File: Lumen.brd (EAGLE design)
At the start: 59.6 x 24 mm, 25 parts, among them J1 AVR_SPI_PRG_6PTH, U1 Tiny45-20-SMT, Y1 8MHZ

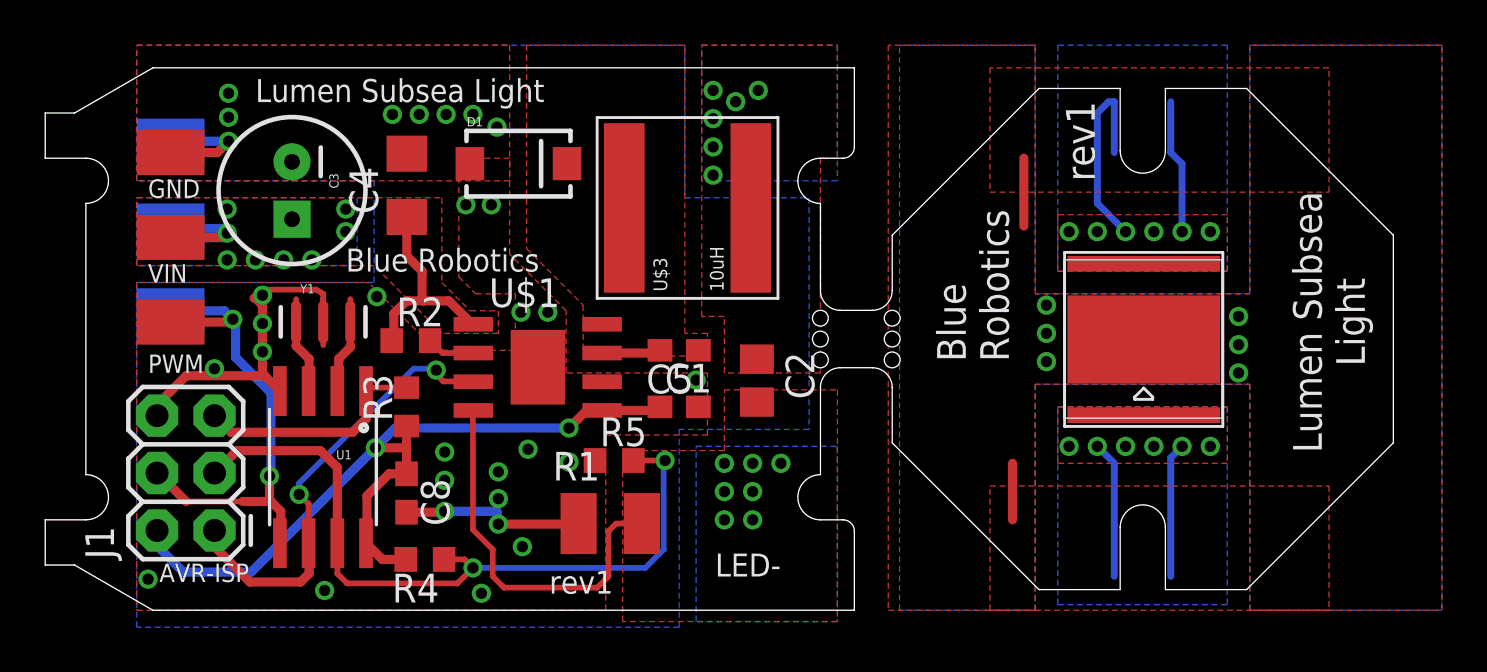
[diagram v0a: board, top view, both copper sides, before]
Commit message: Fixed a lot of little things. Added regulator back into the design. Upgrade capacitor voltage ratings.
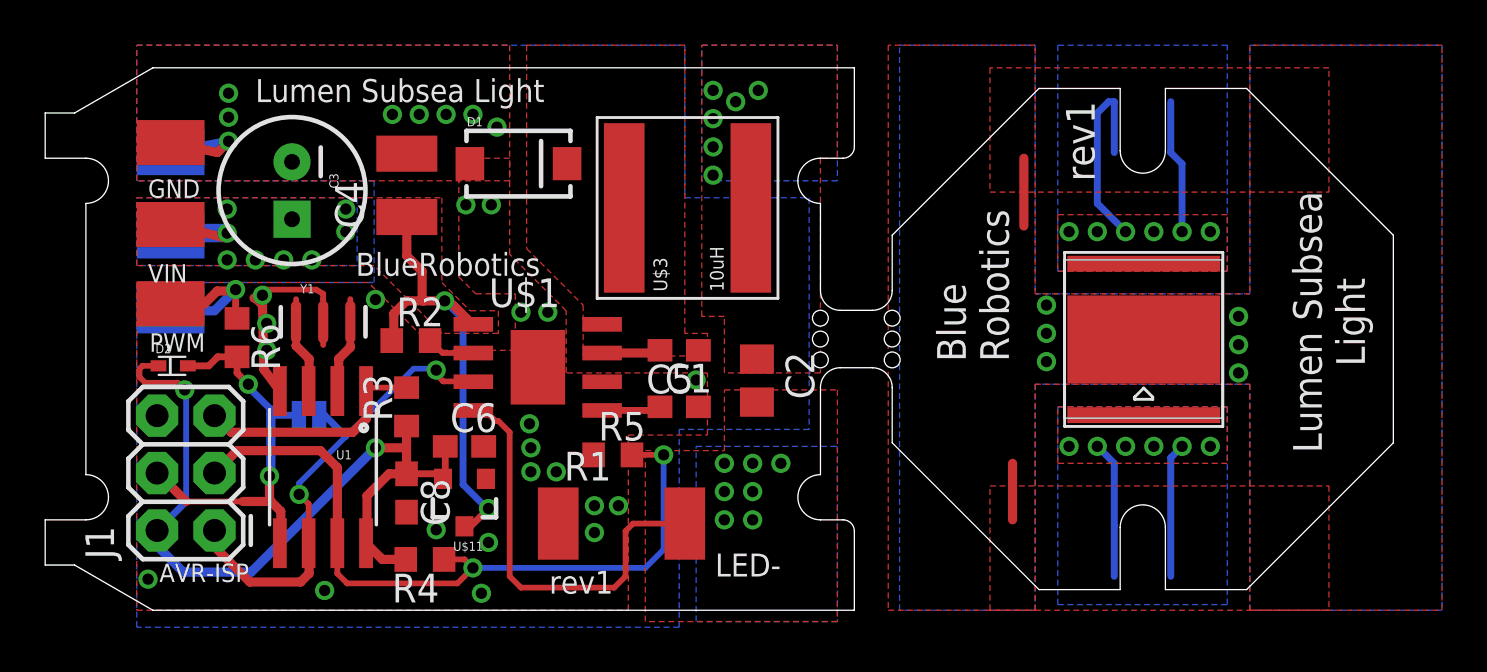
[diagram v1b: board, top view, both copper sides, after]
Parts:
- added C6: 10uF, resistor:C0603
- added D2: (no value), SparkFun-DiscreteSemi:SOD523
- added R6: 27K, resistor:R0603
- added SJ1: JUMPER-PAD-2-NO, SparkFun-Passives:PAD-JUMPER-2-NO_NO_SILK
- added U$11: VREG-ZXTR2105, BlueRobotics-Main:SOT23-3
- C2: value 0.68uF 50V -> 0.68uF 100V
- C4: value 4.7uF 50V -> 4.7uF 80V; device resistor:C1206 -> resistor:C1210
- D1: value 50V 3A -> 60V 3A
- R1: value 0.068 1W -> 0.082 1W; device resistor:R1210 -> resistor:R2512
- moved U$7 0.81 mm to (3.75, 13.6)
- moved U$8 0.56 mm to (3.75, 17.1)
- moved R1 0.50 mm to (23.7, 3.83)
- moved U$6 0.50 mm to (3.75, 20.2)
- moved U$5 0.44 mm to (3.75, 16.6)
- moved U$9 0.44 mm to (3.75, 20.7)
- moved R5 0.26 mm to (23.3, 6.88)
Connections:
- new net SIGNAL_HV: R6.1, U$4.P$1, U$7.P$1
- new net VCC6211: C1.1, U$1.5
- net GND: now also C6.2, U$11.1
- net LED-PWM: now also SJ1.2
- net SIGNAL: now also D2.A, R6.2, SJ1.1; no longer U$4.P$1, U$7.P$1
- net VCC: now also C6.1, D2.C, U$11.2; no longer C1.1, U$1.5
- net VIN: now also U$11.3
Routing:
- net GND: track 27.3 -> 13.9 mm, vias 30 -> 29
- net VIN: track 14.6 -> 27.7 mm, vias 8 -> 10
- net SIGNAL_HV: track 0.00 -> 7.70 mm, vias 0 -> 1
- net SIGNAL: track 22.1 -> 18.3 mm
- net VCC6211: track 0.00 -> 2.63 mm
- net LED-: track 16.9 -> 18.9 mm
- net LED-PWM: track 20.0 -> 21.6 mm
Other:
- board text added: "BlueRobotics"
- board text added: "Direct Signal to A6211"

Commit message: Fixed some layout issues per John's suggestion. Added pads for a snubber that will probably not be populated.
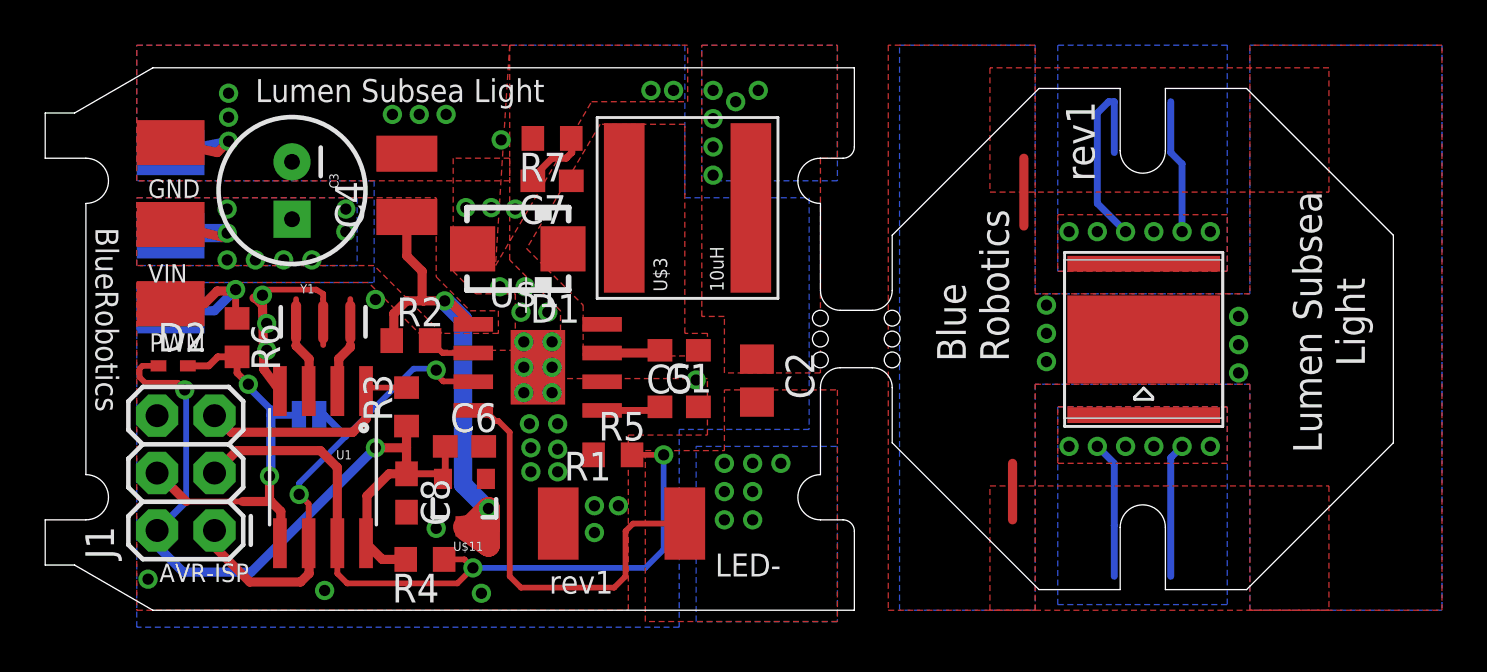
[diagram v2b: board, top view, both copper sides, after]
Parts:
- added C7: NP, resistor:C0603
- added R7: NP, resistor:R0603
- D1: device SparkFun-DiscreteSemi:SMA-DIODE -> BlueRobotics-Main:SMA
- D2: value (none) -> BAT54; device SparkFun-DiscreteSemi:SOD523 -> BlueRobotics-Main:SOD523
- moved D1 3.77 mm to (19.1, 16.0), turned to 180 degrees
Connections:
- new net N$2: C7.2, R7.1
- net GND: now also R7.2
- net N$5: now also C7.1
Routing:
- net VIN: track 27.7 -> 31.6 mm
- net N$2: track 0.00 -> 2.97 mm
- net GND: vias 29 -> 40
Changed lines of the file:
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@@
 <setting verticaltext="up"/>
 </settings>
-<grid distance="5" unitdist="mm" unit="mm" style="lines" multiple="1" display="yes" altdistance="0.0625" altunitdist="mm" altunit="mm"/>
+<grid distance="5" unitdist="mm" unit="mm" style="lines" multiple="1" display="yes" altdistance="0.125" altunitdist="mm" altunit="mm"/>
 <layers>
 <layer number="1" name="Top" color="4" fill="1" visible="yes" active="yes"/>
@@
 <text x="7.5" y="23.5" size="1.016" layer="21" align="top-left">Lumen Subsea Light</text>
 <text x="20.5" y="1.75" size="1.016" layer="21" align="top-left">rev1</text>
-<text x="11.9375" y="15.8125" size="1.016" layer="21" align="top-left">BlueRobotics</text>
+<text x="1.4375" y="16.9375" size="1.016" layer="21" rot="SR270" align="top-left">BlueRobotics</text>
 <text x="48" y="6.25" size="1.016" layer="22" rot="MR0" align="top-left">LED-</text>
 <text x="45.5" y="17.75" size="1.016" layer="22" rot="SMR180" align="top-left">LED+</text>
@@
 <element name="C4" library="resistor" package="C1210" value="4.7uF 80V" x="14.2" y="18.8" rot="R90"/>
 <element name="C5" library="resistor" package="C0603" value="0.1uF" x="26.25" y="11.5" rot="R180"/>
-<element name="D1" library="SparkFun-DiscreteSemi" package="SMA-DIODE" value="60V 3A" x="19.14" y="19.76">
-<attribute name="PROD_ID" value="DIO-09886" x="19.14" y="19.76" size="1.778" layer="27" display="off"/>
-</element>
+<element name="D1" library="BlueRobotics-Main" package="SMA" value="60V 3A" x="19.11" y="15.99" rot="R180"/>
 <element name="J1" library="SparkFun-Connectors" package="2X3" value="AVR_SPI_PRG_6PTH" x="5.69" y="3.53" smashed="yes" rot="R90">
 <attribute name="NAME" x="1.245" y="2.26" size="1.27" layer="25" ratio="10" rot="R90"/>
@@
 <element name="C6" library="resistor" package="C0603" value="10uF" x="16.75" y="7.25"/>
 <element name="SJ1" library="SparkFun-Passives" package="PAD-JUMPER-2-NO_NO_SILK" value="JUMPER-PAD-2-NO" x="9.875" y="8.625" rot="MR180"/>
-<element name="D2" library="SparkFun-DiscreteSemi" package="SOD523" value="" x="3.8125" y="10.8125"/>
+<element name="D2" library="BlueRobotics-Main" package="SOD523" value="BAT54" x="3.8125" y="10.8125"/>
 <element name="R6" library="resistor" package="R0603" value="27K" x="6.6875" y="12.0625" rot="R270"/>
+<element name="C7" library="resistor" package="C0603" value="NP" x="20.625" y="19" rot="R180"/>
+<element name="R7" library="resistor" package="R0603" value="NP" x="20.625" y="20.875" rot="R180"/>
 </elements>
 <signals>
@@
 <wire x1="6.3125" y1="20.75" x2="3.75" y2="20.25" width="0.4064" layer="16"/>
 <via x="13.5625" y="21.9375" extent="1-16" drill="0.5"/>
-<via x="17.125" y="21.9375" extent="1-16" drill="0.5"/>
+<via x="18.375" y="20.8125" extent="1-16" drill="0.5"/>
 <via x="14.75" y="21.9375" extent="1-16" drill="0.5"/>
 <via x="15.9375" y="21.9375" extent="1-16" drill="0.5"/>
-<via x="18.1875" y="21.375" extent="1-16" drill="0.5"/>
-<via x="16.8125" y="17.9375" extent="1-16" drill="0.5"/>
-<via x="17.9375" y="17.9375" extent="1-16" drill="0.5"/>
+<via x="16.8125" y="17.8125" extent="1-16" drill="0.5"/>
+<via x="17.9375" y="17.8125" extent="1-16" drill="0.5"/>
 <via x="6.3125" y="21.8125" extent="1-16" drill="0.5"/>
 <via x="6.3125" y="22.875" extent="1-16" drill="0.5"/>
 <via x="12.8125" y="13.75" extent="1-16" drill="0.5"/>
 <via x="8" y="11.5" extent="1-16" drill="0.5"/>
-<via x="15.5" y="3.5625" extent="1-16" drill="0.5"/>
+<via x="15.5" y="3.625" extent="1-16" drill="0.5"/>
 <via x="22.5" y="3.4375" extent="1-16" drill="0.5"/>
 <via x="19.6875" y="7.1875" extent="1-16" drill="0.5"/>
@@
 <via x="17.5" y="0.75" extent="1-16" drill="0.5"/>
 <polygon width="0.4064" layer="1" isolate="0.254" thermals="no">
-<vertex x="16.5" y="20"/>
-<vertex x="16.5" y="14.75"/>
+<vertex x="16.25" y="20"/>
+<vertex x="16.25" y="15"/>
 <vertex x="17.25" y="14"/>
 <vertex x="19" y="14"/>
@@
 <vertex x="24" y="7.75"/>
 <vertex x="27.5" y="7.75"/>
-<vertex x="27.5" y="10.5"/>
-<vertex x="21.25" y="10.5"/>
-<vertex x="21.25" y="13.25"/>
-<vertex x="18.75" y="15.75"/>
+<vertex x="27.5" y="10.25"/>
+<vertex x="21" y="10.25"/>
+<vertex x="21" y="13.25"/>
+<vertex x="18.75" y="15.5"/>
 <vertex x="18.75" y="20"/>
 </polygon>
@@
 <via x="23.5625" y="4.625" extent="1-16" drill="0.5"/>
 <via x="19.625" y="8.25" extent="1-16" drill="0.5"/>
-<via x="17.8125" y="3" extent="1-16" drill="0.5"/>
 <contactref element="C6" pad="2"/>
-<via x="20.8125" y="6.125" extent="1-16" drill="0.5"/>
+<via x="20.875" y="6.125" extent="1-16" drill="0.5"/>
+<polygon width="0.3048" layer="1" isolate="0.254">
+<vertex x="18.125" y="15.25"/>
+<vertex x="22.375" y="22.5"/>
+<vertex x="26.625" y="22.5"/>
+<vertex x="26.625" y="25"/>
+<vertex x="18.75" y="25"/>
+</polygon>
+<via x="19" y="17.75" extent="1-16" drill="0.5"/>
+<via x="25" y="23" extent="1-16" drill="0.5"/>
+<via x="26" y="23" extent="1-16" drill="0.5"/>
+<via x="19.375" y="9.625" extent="1-16" drill="0.5"/>
+<via x="19.375" y="10.75" extent="1-16" drill="0.5"/>
+<via x="19.375" y="11.875" extent="1-16" drill="0.5"/>
+<via x="20.625" y="11.875" extent="1-16" drill="0.5"/>
+<via x="20.625" y="10.75" extent="1-16" drill="0.5"/>
+<via x="20.625" y="9.625" extent="1-16" drill="0.5"/>
+<via x="20.875" y="8.25" extent="1-16" drill="0.5"/>
+<via x="20.875" y="7.125" extent="1-16" drill="0.5"/>
+<via x="19.4375" y="14.3125" extent="1-16" drill="0.5"/>
+<via x="18.3125" y="14.3125" extent="1-16" drill="0.5"/>
+<contactref element="R7" pad="2"/>
 </signal>
 <signal name="N$1">
@@
 <polygon width="0.4064" layer="1" isolate="0.254" thermals="no">
 <vertex x="2.25" y="18.25"/>
-<vertex x="15.75" y="18.25"/>
-<vertex x="15.75" y="14.5"/>
+<vertex x="15.5" y="18.25"/>
+<vertex x="15.5" y="14.75"/>
 <vertex x="17" y="13.25"/>
 <vertex x="18.25" y="13.25"/>
@@
 <contactref element="U$11" pad="3"/>
 <wire x1="16.75" y1="3.7125" x2="17.025" y2="3.7125" width="0.3048" layer="1"/>
-<wire x1="17.025" y1="3.7125" x2="17.8125" y2="4.5" width="0.3048" layer="1"/>
+<wire x1="17.025" y1="3.7125" x2="17.8125" y2="4.5" width="1.016" layer="1"/>
 <via x="17.8125" y="4.5" extent="1-16" drill="0.5"/>
 <wire x1="17.8125" y1="4.5" x2="17.75" y2="4.5" width="0.3048" layer="16"/>
-<wire x1="17.75" y1="4.5" x2="16.6875" y2="5.5625" width="0.3048" layer="16"/>
-<wire x1="16.6875" y1="5.5625" x2="16.6875" y2="12.875" width="0.3048" layer="16"/>
-<wire x1="16.6875" y1="12.875" x2="15.875" y2="13.6875" width="0.3048" layer="16"/>
+<wire x1="17.75" y1="4.5" x2="16.6875" y2="5.5625" width="0.8128" layer="16"/>
+<wire x1="16.6875" y1="5.5625" x2="16.6875" y2="12.875" width="0.8128" layer="16"/>
+<wire x1="16.6875" y1="12.875" x2="15.875" y2="13.6875" width="0.8128" layer="16"/>
 <via x="15.875" y="13.6875" extent="1-16" drill="0.5"/>
 <wire x1="15.875" y1="13.6875" x2="16.1025" y2="13.6875" width="0.3048" layer="1"/>
 <wire x1="16.1025" y1="13.6875" x2="17.14" y2="12.65" width="0.3048" layer="1"/>
+<wire x1="16.75" y1="3.6875" x2="17.8125" y2="3.6875" width="1.016" layer="1"/>
+<wire x1="17.8125" y1="4.5" x2="17.8125" y2="2.875" width="1.016" layer="1"/>
+<wire x1="17.8125" y1="2.875" x2="16.8125" y2="3.5625" width="1.016" layer="1"/>
+<wire x1="16.75" y1="3.6875" x2="16.75" y2="3.7125" width="0.8128" layer="1"/>
 </signal>
 <signal name="LED-PWM">
@@
 <vertex x="27.5" y="12.25"/>
 <vertex x="26.5" y="12.25"/>
-<vertex x="26.5" y="25"/>
-<vertex x="19.5" y="25"/>
+<vertex x="26.5" y="21.5"/>
+<vertex x="22.75" y="21.5"/>
 <vertex x="19.5" y="16"/>
 <vertex x="22" y="13.5"/>
 <vertex x="22" y="11.25"/>
 </polygon>
+<contactref element="C7" pad="1"/>
 </signal>
 <signal name="LED+">
@@
 <wire x1="6.5625" y1="14.125" x2="6.625" y2="14.1875" width="0.3048" layer="1"/>
 </signal>
+<signal name="N$2">
+<contactref element="R7" pad="1"/>
+<contactref element="C7" pad="2"/>
+<wire x1="19.775" y1="19" x2="19.775" y2="19.15" width="0.3048" layer="1"/>
+<wire x1="19.775" y1="19.15" x2="20.625" y2="20" width="0.3048" layer="1"/>
+<wire x1="20.625" y1="20" x2="21.25" y2="20" width="0.3048" layer="1"/>
+<wire x1="21.25" y1="20" x2="21.5" y2="20.25" width="0.3048" layer="1"/>
+<wire x1="21.5" y1="20.25" x2="21.5" y2="20.85" width="0.3048" layer="1"/>
+<wire x1="21.5" y1="20.85" x2="21.475" y2="20.875" width="0.3048" layer="1"/>
+</signal>
 </signals>

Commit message: More updates based on J.N. comments. Ready to order I believe.
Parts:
- R7: device resistor:R0603 -> resistor:R1206
- moved R7 0.79 mm to (19.9, 21.1)
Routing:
- net EXT: track 5.50 -> 9.38 mm, vias 6 -> 22
- net VCC: track 36.5 -> 34.1 mm
- net GND: track 13.9 -> 15.1 mm, vias 40 -> 43
- net VIN: track 31.6 -> 32.7 mm, vias 10 -> 11
- net LED-: track 18.9 -> 18.4 mm
- net LED-ISO: track 14.9 -> 14.8 mm, vias 6 -> 14
- net LED+ISO: track 12.0 -> 11.9 mm, vias 6 -> 14
- added copper zone on layer 1, net VCC
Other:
- board text added: "Direct PWM to A6211"
- board text added: "R.J. 12/15"
- board text removed: "Direct Signal to A6211"
